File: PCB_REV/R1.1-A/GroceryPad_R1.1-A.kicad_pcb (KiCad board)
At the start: 2 copper layers, 66.2 x 36 mm, 6 parts, among them SW1 SW_SPST, U1 ESP32-C3_SUPERMINI_TH

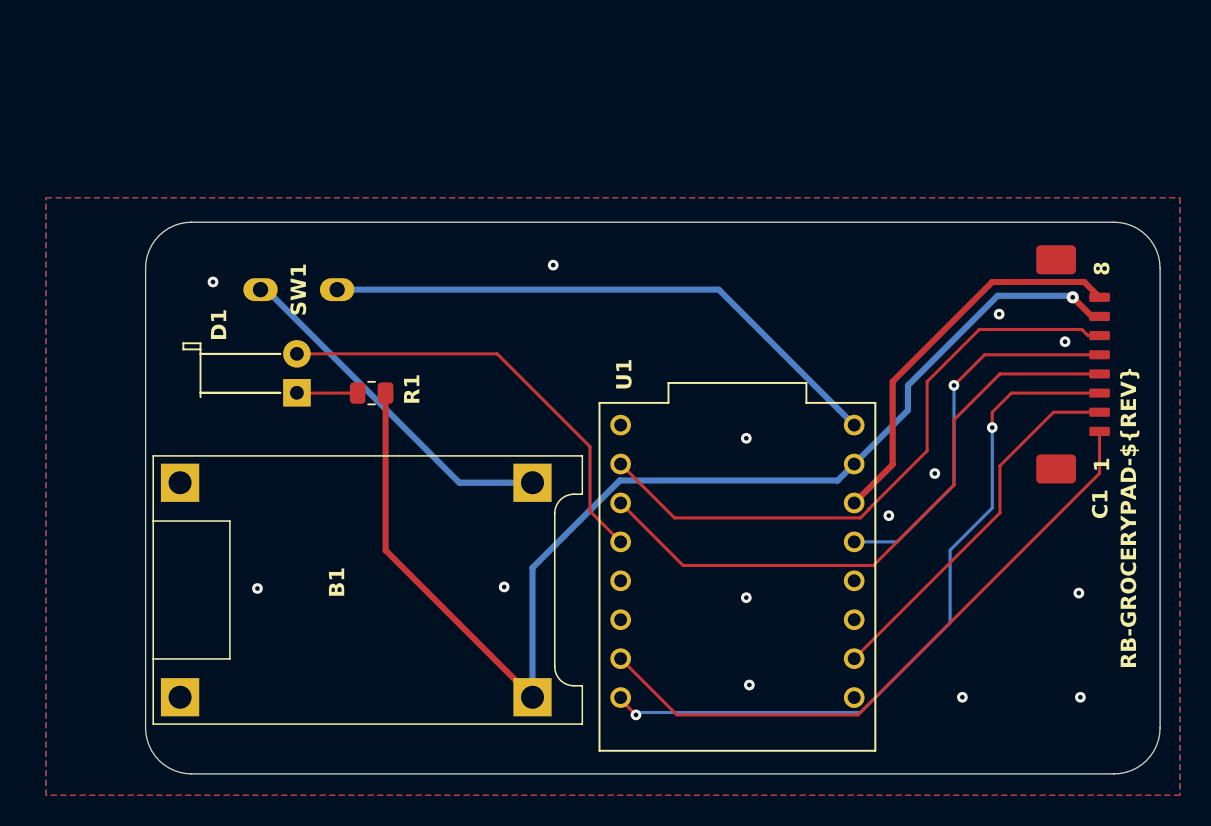
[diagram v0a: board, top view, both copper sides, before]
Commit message: Power switch and case update
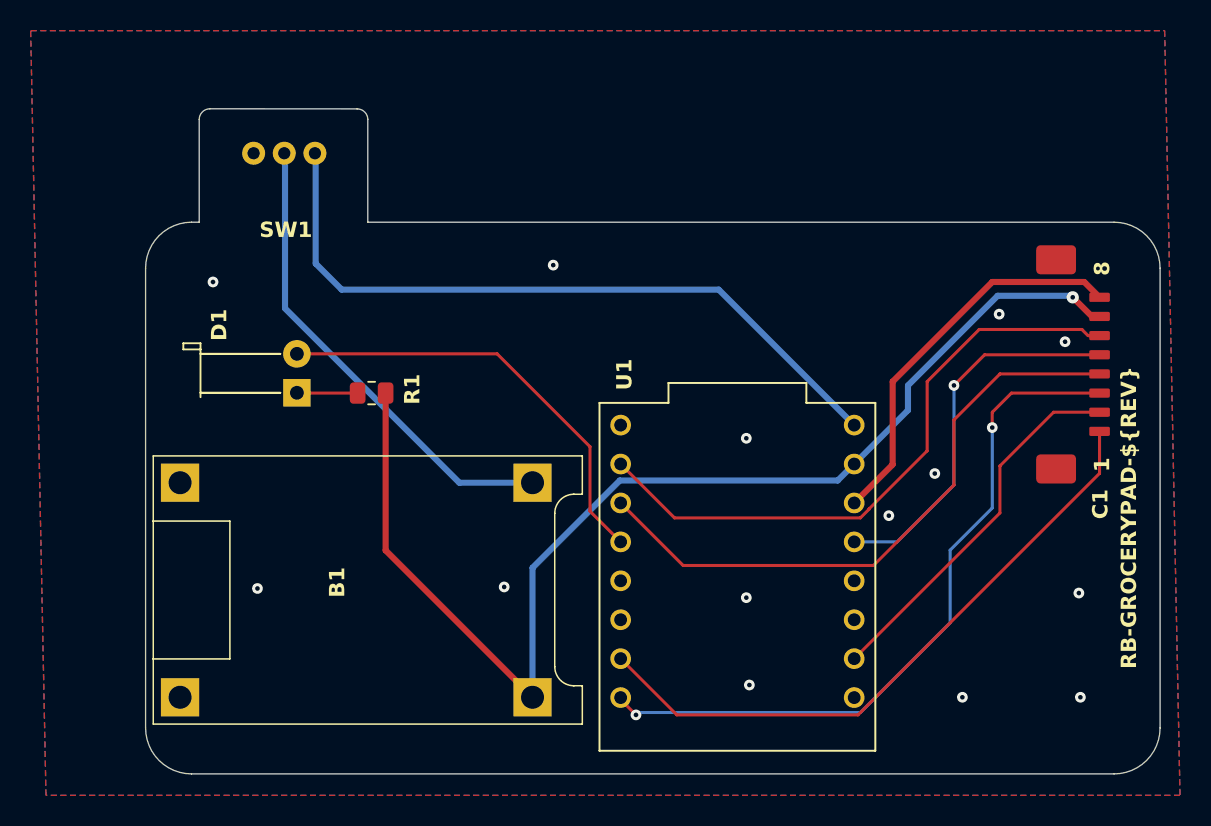
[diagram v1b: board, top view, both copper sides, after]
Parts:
- SW1: value SW_SPST -> SW_SPDT_312; footprint Switch:SPST Switch -> Switch:SPDT Slide Switch
- moved SW1 8.95 mm to (196.6, 104.1)
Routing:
- net SW_5V: track 37.4 -> 46.7 mm
- net 5V: track 23.0 -> 31.0 mm
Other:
- board size 66.2 x 36 mm -> 66.2 x 43.4 mm
